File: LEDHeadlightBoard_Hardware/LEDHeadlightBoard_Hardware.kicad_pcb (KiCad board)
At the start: 2 copper layers, 12 x 16.5 mm, 6 parts, among them J1 Solder_Pad, J2 Solder_Pad

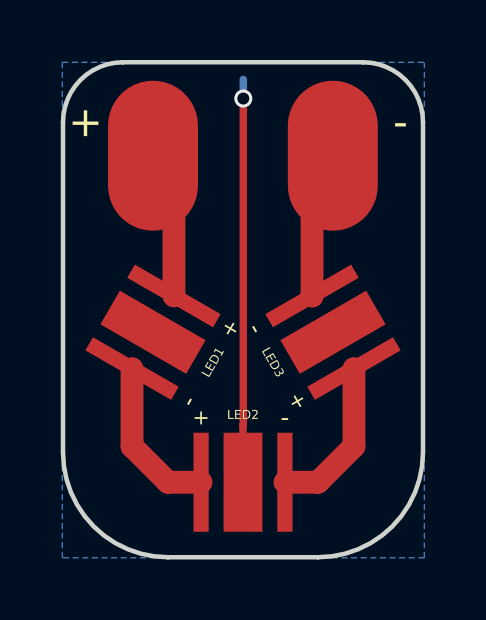
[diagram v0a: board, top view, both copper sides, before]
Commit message: Rev.1 Layout Finished
Meant for use with Cree XLamp XP-G2 LEDs (XPGBWT-L1-0000-00H53)
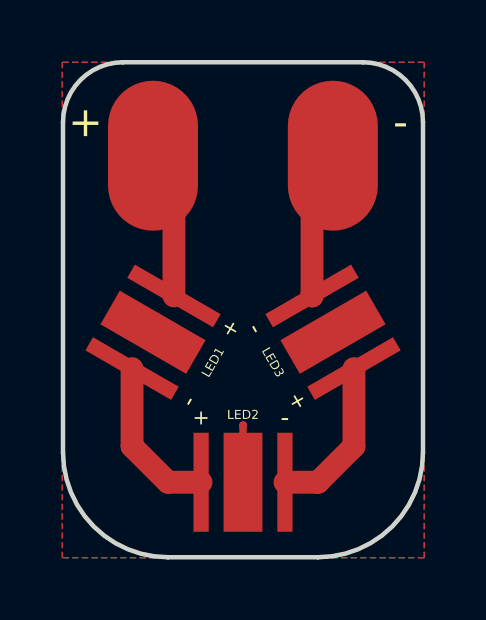
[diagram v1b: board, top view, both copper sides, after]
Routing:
- net /Heat_Slug: track 13.4 -> 1.92 mm, vias 1 -> 0
- added copper zone on B.Cu, net (none)
- added copper zone on F.Cu, net /Heat_Slug
- removed copper zone on B.Cu, net /Heat_Slug
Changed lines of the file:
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@@
   (general
     (links 6)
-    (no_connects 2)
+    (no_connects 0)
     (area 136.5456 89.92 149.575001 108.075001)
     (thickness 1.6)
     (drawings 10)
-    (tracks 16)
+    (tracks 13)
     (zones 0)
     (modules 6)
@@
   (segment (start 145.8015 95.1938) (end 146.4989 94.4964) (width 0.762) (layer F.Cu) (net 2))
   (segment (start 145.8015 99.290163) (end 145.8015 99.1985) (width 0.762) (layer F.Cu) (net 2))
-  (segment (start 143.51 92.71) (end 143.51 92.075) (width 0.25) (layer B.Cu) (net 3))
-  (segment (start 143.51 103.589) (end 143.51 92.71) (width 0.25) (layer F.Cu) (net 3))
-  (via (at 143.51 92.71) (size 0.6) (drill 0.4) (layers F.Cu B.Cu) (net 3))
   (segment (start 143.5 105.5) (end 143.5 103.599) (width 0.25) (layer F.Cu) (net 3))
   (segment (start 143.5 103.599) (end 143.51 103.589) (width 0.25) (layer F.Cu) (net 3))
@@
   (segment (start 146 105.5) (end 144.897 105.5) (width 0.762) (layer F.Cu) (net 5))
   (segment (start 147.1985 104.3015) (end 146 105.5) (width 0.762) (layer F.Cu) (net 5))
-  (zone (net 3) (net_name /Heat_Slug) (layer B.Cu) (hatch edge 0.508)
+  (zone (net 0) (net_name "") (layer B.Cu) (hatch edge 0.508)
     (connect_pads yes (clearance 0))
     (min_thickness 0.2)
@@
       )
     )
+  )
+  (zone (net 3) (net_name /Heat_Slug) (layer F.Cu) (hatch edge 0.508)
+    (connect_pads yes (clearance 0))
+    (min_thickness 0.2)
+    (fill yes (arc_segments 16) (thermal_gap 0.508) (thermal_bridge_width 0.508))
+    (polygon
+      (pts
+        (xy 149.5425 108.0135) (xy 149.5425 91.5035) (xy 137.4775 91.5035) (xy 137.4775 108.0135)
+      )
+    )
